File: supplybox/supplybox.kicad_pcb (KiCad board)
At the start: 2 copper layers, 75 x 85 mm, 56 parts, among them U1 EPM1210SJ_1212AE, U2 MC33063AD, U3 MC33063AD

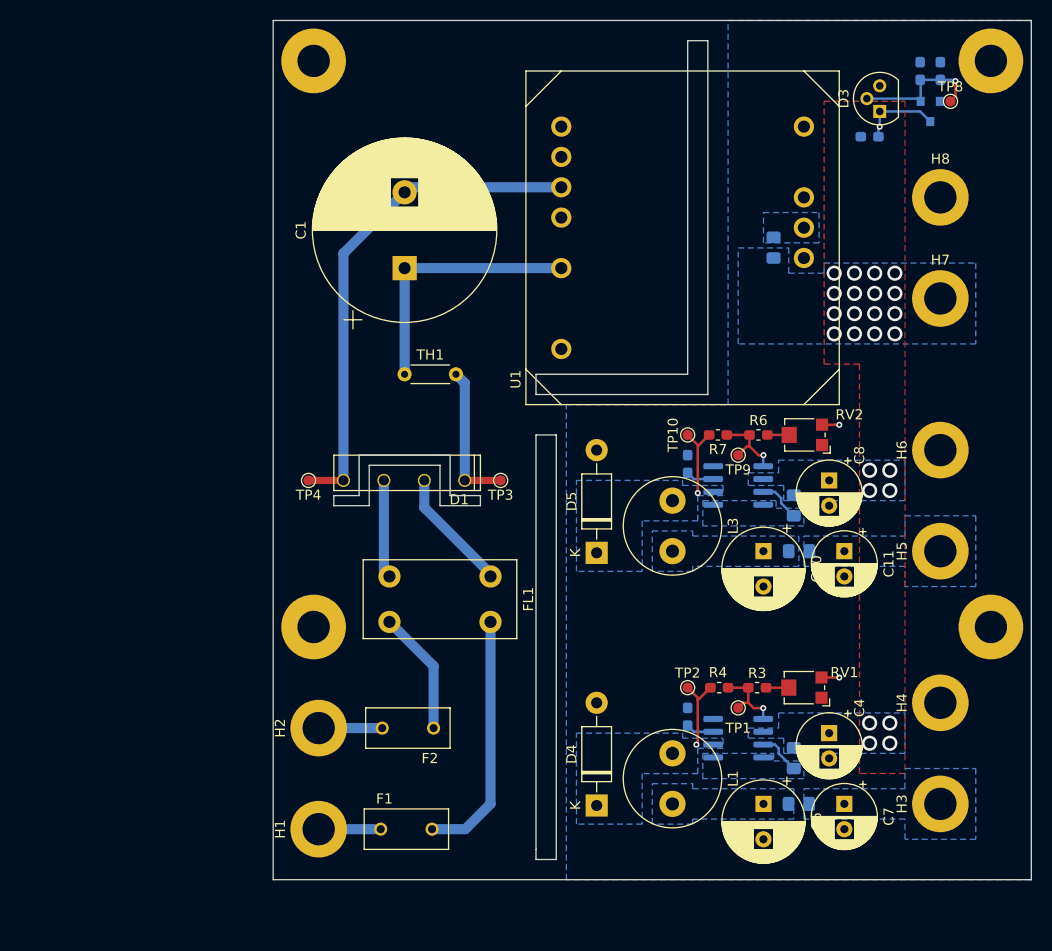
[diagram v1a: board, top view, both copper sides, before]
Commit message: redo pcb and fix issues with schematic
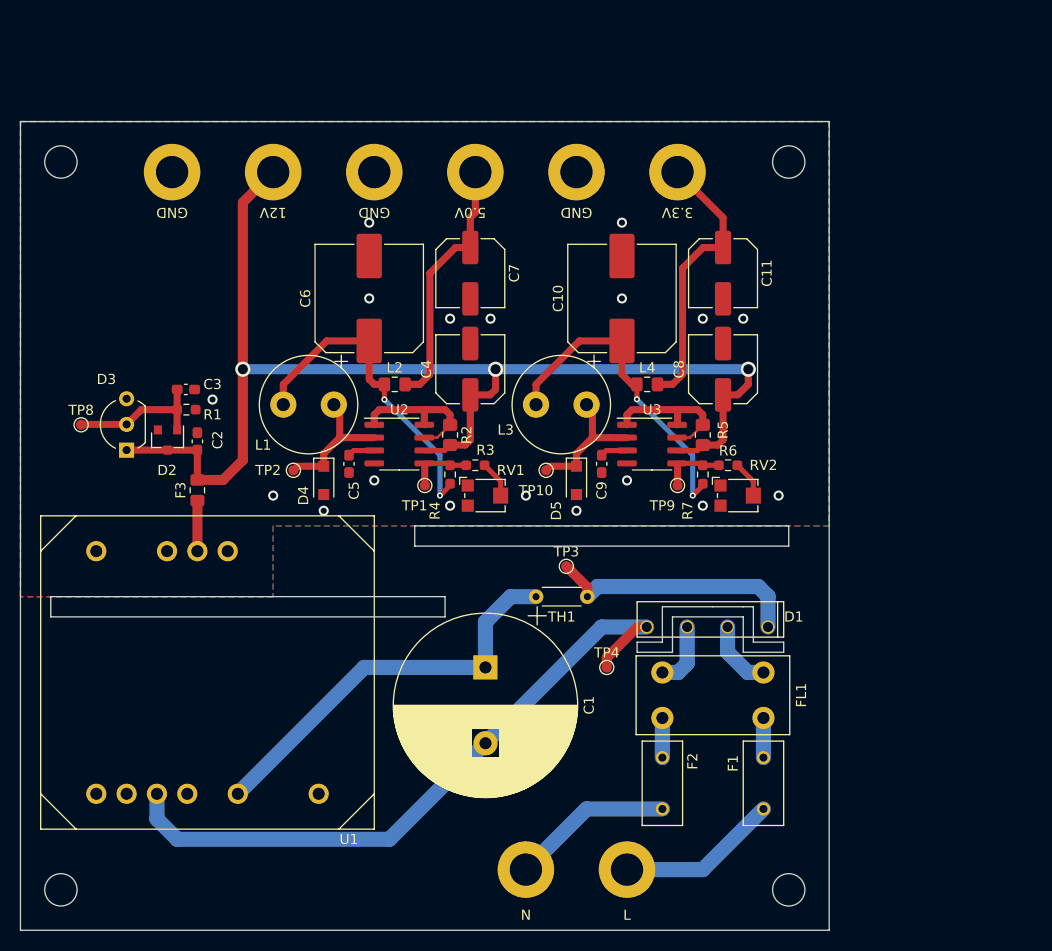
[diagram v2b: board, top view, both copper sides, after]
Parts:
- removed the REF** at (109.0, 70.0)
- removed the REF** at (176.0, 70.0)
- removed the REF** at (176.0, 14.0)
- removed the REF** at (109.0, 14.0)
- added REF**: MountingHole_3.2mm_M3_DIN965, MountingHole:MountingHole_3.2mm_M3_DIN965, F.Cu at (156.0, 24.0)
- added REF**: MountingHole_3.2mm_M3_DIN965, MountingHole:MountingHole_3.2mm_M3_DIN965, F.Cu at (84.0, 24.0)
- added REF**: MountingHole_3.2mm_M3_DIN965, MountingHole:MountingHole_3.2mm_M3_DIN965, F.Cu at (84.0, 96.0)
- added REF**: MountingHole_3.2mm_M3_DIN965, MountingHole:MountingHole_3.2mm_M3_DIN965, F.Cu at (156.0, 96.0)
- C10, C6: footprint Capacitor_THT:CP_Radial_D8.0mm_P3.50mm -> Capacitor_SMD:CP_Elec_10x10.5
- C11, C4, C7, C8: footprint Capacitor_THT:CP_Radial_D6.3mm_P2.50mm -> Capacitor_SMD:C_Elec_6.3x7.7
- C2, C3, C5, C9: footprint Capacitor_SMD:C_0603_1608Metric_Pad1.05x0.95mm_HandSolder -> Capacitor_SMD:C_0603_1608Metric_Pad1.08x0.95mm_HandSolder; moved to F.Cu
- D2, F3, L2, L4, U2, U3: moved to F.Cu
- D3: footprint Package_TO_SOT_THT:TO-92 -> Package_TO_SOT_THT:TO-92_Inline_Wide
- D4, D5: footprint Diode_THT:D_DO-41_SOD81_P10.16mm_Horizontal -> Diode_SMD:D_SOD-123F
- F1, F2: value 100mA -> 2.5A
- R1: footprint Resistor_SMD:R_0603_1608Metric_Pad1.05x0.95mm_HandSolder -> Resistor_SMD:R_0603_1608Metric_Pad0.98x0.95mm_HandSolder; moved to F.Cu
- R2, R5: footprint Resistor_SMD:R_0805_2012Metric_Pad1.15x1.40mm_HandSolder -> Resistor_SMD:R_0805_2012Metric_Pad1.20x1.40mm_HandSolder; moved to F.Cu
- R3: value R -> 1200; footprint Resistor_SMD:R_0603_1608Metric_Pad1.05x0.95mm_HandSolder -> Resistor_SMD:R_0603_1608Metric_Pad0.98x0.95mm_HandSolder
- R4, R7: value R -> 3900; footprint Resistor_SMD:R_0603_1608Metric_Pad1.05x0.95mm_HandSolder -> Resistor_SMD:R_0603_1608Metric_Pad0.98x0.95mm_HandSolder
- R6: value R -> 2200; footprint Resistor_SMD:R_0603_1608Metric_Pad1.05x0.95mm_HandSolder -> Resistor_SMD:R_0603_1608Metric_Pad0.98x0.95mm_HandSolder
- moved TP8 91.8 mm to (86.0, 50.0)
- moved D2 82.2 mm to (94.5, 51.5)
- moved R1 81.8 mm to (96.4, 48.5), turned to 0 degrees
- moved D3 81.7 mm to (90.5, 52.5)
- moved C3 79.2 mm to (96.4, 46.5), turned to 0 degrees
- moved H3 77.6 mm to (125.0, 25.0), turned to 0 degrees
- moved H4 76.8 mm to (115.0, 25.0), turned to 0 degrees
- moved H8 76.0 mm to (95.0, 25.0)
- moved C2 73.0 mm to (97.5, 51.6), turned to 90 degrees
- moved H7 67.2 mm to (105.0, 25.0)
- moved C7 64.2 mm to (124.5, 35.0)
- moved C6 63.4 mm to (114.5, 37.5), turned to 90 degrees
- moved F3 61.8 mm to (97.5, 56.5), turned to 90 degrees
- moved L2 57.6 mm to (117.0, 46.0)
- moved C4 50.6 mm to (124.5, 44.5), turned to 90 degrees
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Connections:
- R4 pad 2: Net-(D4-Pad1) -> Net-(C6-Pad1)
- R7 pad 2: Net-(D5-Pad1) -> Net-(C10-Pad1)
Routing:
- net +12V: track 8.14 -> 123.0 mm, vias 25 -> 3
- net Net-(C6-Pad1): track 0.00 -> 32.7 mm, vias 0 -> 2
- net Net-(C10-Pad1): track 0.00 -> 32.3 mm, vias 0 -> 2
- net +3V3: track 0.00 -> 27.6 mm
- net +5V: track 0.00 -> 25.6 mm
- net /L_Fused: track 24.8 -> 3.92 mm
- net /DC-: track 50.2 -> 66.7 mm
- net /DC+L: track 26.0 -> 40.2 mm
- net /DC+: track 14.4 -> 25.6 mm
- net LINE: track 5.50 -> 16.0 mm
- net Net-(R5-Pad1): track 4.30 -> 14.5 mm
- net Net-(R2-Pad1): track 4.30 -> 14.5 mm
- net NEUT: track 6.28 -> 16.0 mm
- net /N_Fused: track 12.3 -> 3.92 mm
- net Net-(D5-Pad1): track 7.72 -> 13.6 mm, vias 1 -> 0
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- added copper zone on F.Cu, net GND
- removed copper zone on B.Cu, net +12V
- removed copper zone on F.Cu, net +12V
- removed copper zone on B.Cu, net +3V3
- removed copper zone on B.Cu, net +5V
- removed copper zone on B.Cu, net /12V_Unfused
- removed copper zone on B.Cu, net Net-(C10-Pad1)
- removed copper zone on B.Cu, net Net-(C6-Pad1)
- removed copper zone on B.Cu, net Net-(D4-Pad1)
- removed copper zone on B.Cu, net Net-(D5-Pad1)
- removed copper zone on B.Cu, net Net-(R2-Pad1)
- removed copper zone on B.Cu, net Net-(R5-Pad1)
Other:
- board size 75 x 85 mm -> 80 x 80 mm
- net class Danger removed
- net class Power removed
- rule trace_min: 0.15 -> 0.127
- rule via_min_drill: 0.3 -> 0.2
- rule via_min_size: 0.4 -> 0.45
- board text added: "12V"
- board text added: "3.3V"
- board text added: "5.0V"
- board text added: "GND"
- board text added: "L"
- board text added: "N"
